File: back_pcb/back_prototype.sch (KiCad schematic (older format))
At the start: 75 parts, among them P1 EXPANSION_LEFT, P2 EXPANSION_BOTTOM, P3 EXPANSION_TOP, P4 USB_A, P5 AUDIO_CONN, P6 ATMEGA_HEADER, P7 EXPANSION_BOTTOM2, P8 JST, P9 USB_A, Q1 IRLML6401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

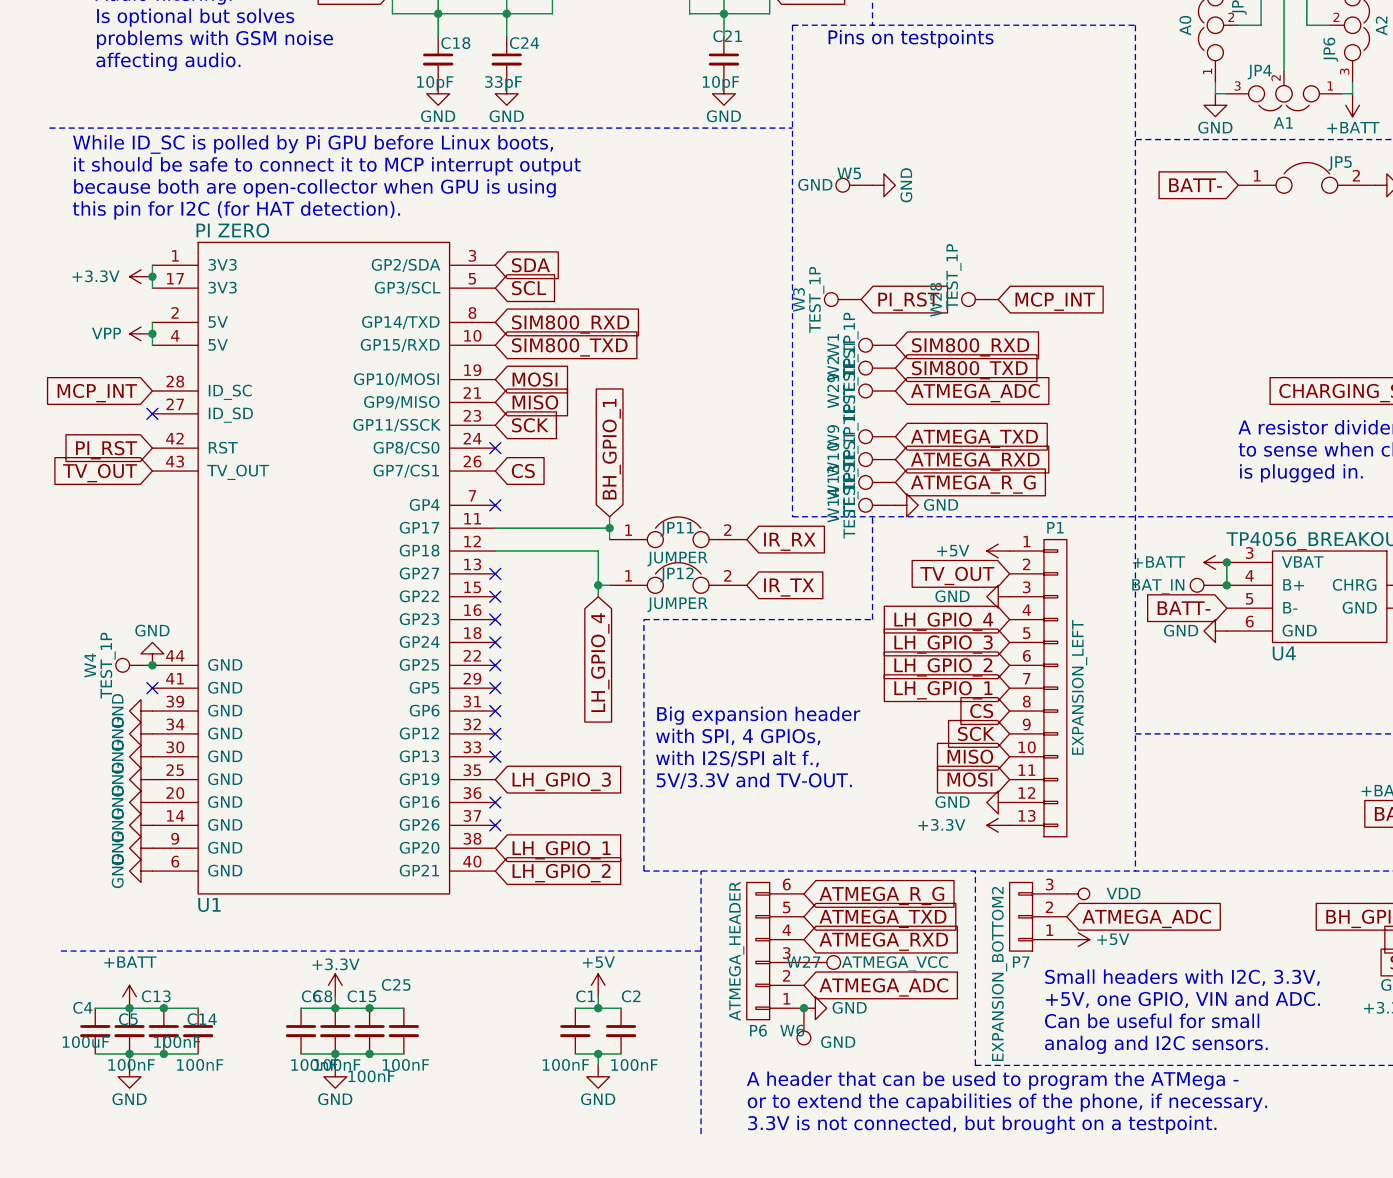
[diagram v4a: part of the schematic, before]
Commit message: Last minute changes in back board
* Added a VSYS capacitor
* Added a capacitor in parallel with the battery
* Removed the MCP_INT testpoint and testpoints for free MCP GPIOs
* Remove the footprint for additional protection IC
* Stitched the board with vias
* Moved the traces around for better grounds
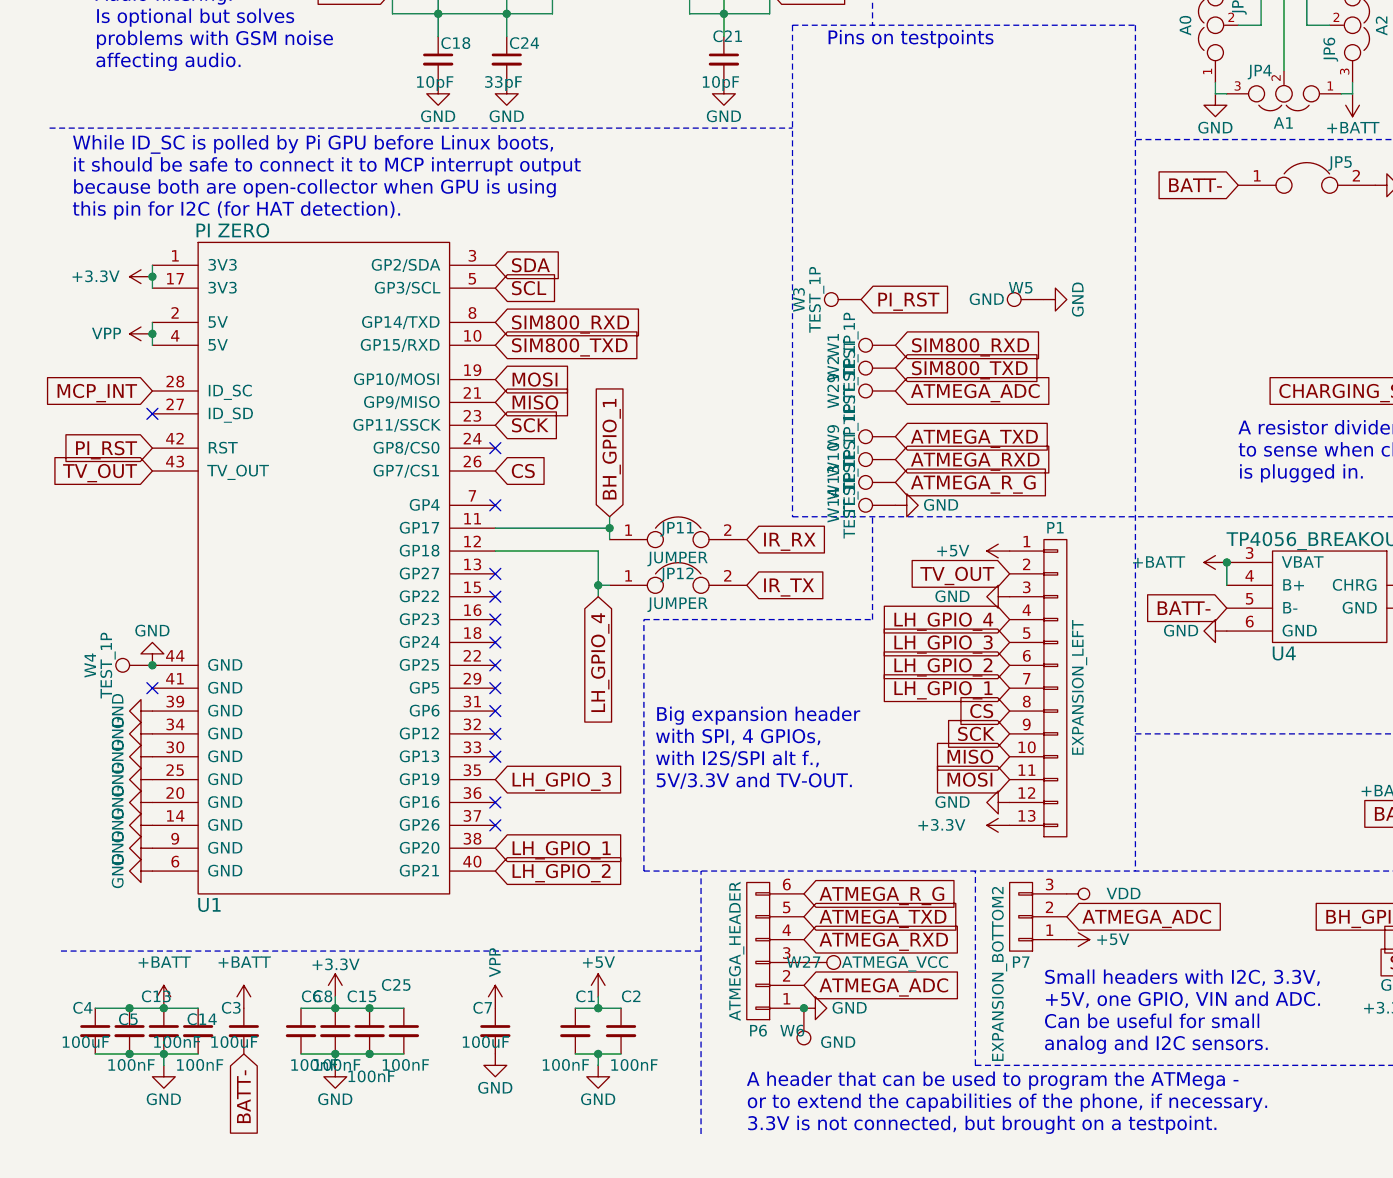
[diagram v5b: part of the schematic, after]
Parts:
- removed W11: BAT_IN, Measurement_Points:Measurement_Point_Square-SMD-Pad_Small, symbol TEST_1P
- removed W28: TEST_1P, Measurement_Points:Measurement_Point_Square-SMD-Pad_Small, symbol TEST_1P
- added C3, C7: 100uF, Capacitors_Tantalum_SMD:CP_Tantalum_Case-B_EIA-3528-21_Hand, symbol C_Small
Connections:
- net +BATT: now also C3.1
- net BATT-: now also C3.2
- net GND: now also C7.2
- net VPP: now also C7.1
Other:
- moved on the sheet: W5
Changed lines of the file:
@@
-	0    -1   -1   0
-$EndComp
-$Comp
-L TEST_1P W11
-U 1 1 5845A9D8
-P 5650 5400
-F 0 "W11" V 5650 5400 50  0001 C CNN
-F 1 "BAT_IN" V 5650 5700 50  0000 C CNN
-F 2 "Measurement_Points:Measurement_Point_Square-SMD-Pad_Small" H 5850 5400 50  0001 C CNN
-F 3 "" H 5850 5400 50  0000 C CNN
-	1    5650 5400
 	0    -1   -1   0
 $EndComp
@@
 L TEST_1P W5
 U 1 1 588B5AFB
-P 4100 3650
-F 0 "W5" V 4150 3750 50  0000 C CNN
-F 1 "GND" V 4100 3900 50  0000 C CNN
-F 2 "Measurement_Points:Measurement_Point_Square-SMD-Pad_Small" H 4300 3650 50  0001 C CNN
-F 3 "" H 4300 3650 50  0000 C CNN
-	1    4100 3650
+P 4850 4150
+F 0 "W5" V 4900 4250 50  0000 C CNN
+F 1 "GND" V 4850 4400 50  0000 C CNN
+F 2 "Measurement_Points:Measurement_Point_Square-SMD-Pad_Small" H 5050 4150 50  0001 C CNN
+F 3 "" H 5050 4150 50  0000 C CNN
+	1    4850 4150
 	0    -1   -1   0
 $EndComp
@@
 $EndComp
 $Comp
-L TEST_1P W28
-U 1 1 588FD363
-P 4650 4150
-F 0 "W28" H 4650 4420 50  0000 C CNN
-F 1 "TEST_1P" H 4750 4350 50  0000 C CNN
-F 2 "Measurement_Points:Measurement_Point_Square-SMD-Pad_Small" H 4850 4150 50  0001 C CNN
-F 3 "" H 4850 4150 50  0000 C CNN
-	1    4650 4150
-	0    -1   -1   0
-$EndComp
-$Comp
 L TEST_1P W29
 U 1 1 588F8B4F
@@
 L GND #PWR050
 U 1 1 58901942
-P 4100 3650
-F 0 "#PWR050" H 4100 3400 50  0001 C CNN
-F 1 "GND" H 4100 3500 50  0000 C CNN
-F 2 "" H 4100 3650 50  0000 C CNN
-F 3 "" H 4100 3650 50  0000 C CNN
-	1    4100 3650
+P 4850 4150
+F 0 "#PWR050" H 4850 3900 50  0001 C CNN
+F 1 "GND" H 4850 4000 50  0000 C CNN
+F 2 "" H 4850 4150 50  0000 C CNN
+F 3 "" H 4850 4150 50  0000 C CNN
+	1    4850 4150
 	0    -1   -1   0
 $EndComp
@@
 Text GLabel 4050 4150 2    60   Input ~ 0
 PI_RST
-Text GLabel 4650 4150 2    60   Input ~ 0
-MCP_INT
 $Comp
 L CONN_01X02 P8
@@
 L +BATT #PWR056
 U 1 1 58911AF4
-P 850 7250
-F 0 "#PWR056" H 850 7100 50  0001 C CNN
-F 1 "+BATT" H 850 7450 50  0000 C CNN
-F 2 "" H 850 7250 50  0000 C CNN
-F 3 "" H 850 7250 50  0000 C CNN
-	1    850  7250
+P 1000 7250
+F 0 "#PWR056" H 1000 7100 50  0001 C CNN
+F 1 "+BATT" H 1000 7450 50  0000 C CNN
+F 2 "" H 1000 7250 50  0000 C CNN
+F 3 "" H 1000 7250 50  0000 C CNN
+	1    1000 7250
 	1    0    0    -1
 $EndComp
@@
 L GND #PWR058
 U 1 1 589168FA
-P 850 7500
-F 0 "#PWR058" H 850 7250 50  0001 C CNN
-F 1 "GND" H 850 7350 50  0000 C CNN
-F 2 "" H 850 7500 50  0000 C CNN
-F 3 "" H 850 7500 50  0000 C CNN
-	1    850  7500
+P 1000 7500
+F 0 "#PWR058" H 1000 7250 50  0001 C CNN
+F 1 "GND" H 1000 7350 50  0000 C CNN
+F 2 "" H 1000 7500 50  0000 C CNN
+F 3 "" H 1000 7500 50  0000 C CNN
+	1    1000 7500
 	1    0    0    -1
 $EndComp
@@
 Wire Wire Line
 	5650 5400 5650 5300
-Connection ~ 5650 5400
 Connection ~ 5650 5300
 Wire Wire Line
@@
 Wire Wire Line
 	8100 6400 8300 6400
-Wire Wire Line
-	700  7250 1150 7250
-Wire Wire Line
-	700  7450 1150 7450
 Wire Wire Line
 	7250 700  7400 700
@@
 Connection ~ 850  7250
 Connection ~ 850  7450
-Wire Wire Line
-	850  7500 850  7450
 Connection ~ 1900 7450
 Connection ~ 1900 7250
@@
 Connection ~ 10100 1650
 Connection ~ 9900 1650
+$Comp
+L C_Small C3
+U 1 1 58D40043
+P 1350 7350
+F 0 "C3" H 1250 7450 50  0000 L CNN
+F 1 "100uF" H 1200 7300 50  0000 L CNN
+F 2 "Capacitors_Tantalum_SMD:CP_Tantalum_Case-B_EIA-3528-21_Hand" H 1350 7350 50  0001 C CNN
+F 3 "" H 1350 7350 50  0000 C CNN
+	1    1350 7350
+	1    0    0    -1
+$EndComp
+$Comp
+L C_Small C7
+U 1 1 58D40155
+P 2450 7350
+F 0 "C7" H 2350 7450 50  0000 L CNN
+F 1 "100uF" H 2300 7300 50  0000 L CNN
+F 2 "Capacitors_Tantalum_SMD:CP_Tantalum_Case-B_EIA-3528-21_Hand" H 2450 7350 50  0001 C CNN
+F 3 "" H 2450 7350 50  0000 C CNN
+	1    2450 7350
+	1    0    0    -1
+$EndComp
+$Comp
+L GND #PWR071
+U 1 1 58D40C19
+P 2450 7450
+F 0 "#PWR071" H 2450 7200 50  0001 C CNN
+F 1 "GND" H 2450 7300 50  0000 C CNN
+F 2 "" H 2450 7450 50  0000 C CNN
+F 3 "" H 2450 7450 50  0000 C CNN
+	1    2450 7450
+	1    0    0    -1
+$EndComp
+$Comp
+L VPP #PWR072
+U 1 1 58D40F5D
+P 2450 7250
+F 0 "#PWR072" H 2450 7100 50  0001 C CNN
+F 1 "VPP" V 2450 7450 50  0000 C CNN
+F 2 "" H 2450 7250 50  0000 C CNN
+F 3 "" H 2450 7250 50  0000 C CNN
+	1    2450 7250
+	1    0    0    -1
+$EndComp
+Wire Wire Line
+	1000 7500 1000 7450
+Wire Wire Line
+	700  7250 1150 7250
+Wire Wire Line
+	1150 7450 700  7450
+$Comp
+L +BATT #PWR073
+U 1 1 58D46D04
+P 1350 7250
+F 0 "#PWR073" H 1350 7100 50  0001 C CNN
+F 1 "+BATT" H 1350 7450 50  0000 C CNN
+F 2 "" H 1350 7250 50  0000 C CNN
+F 3 "" H 1350 7250 50  0000 C CNN
+	1    1350 7250
+	1    0    0    -1
+$EndComp
+Text GLabel 1350 7450 3    60   Input ~ 0
+BATT-
 $EndSCHEMATC

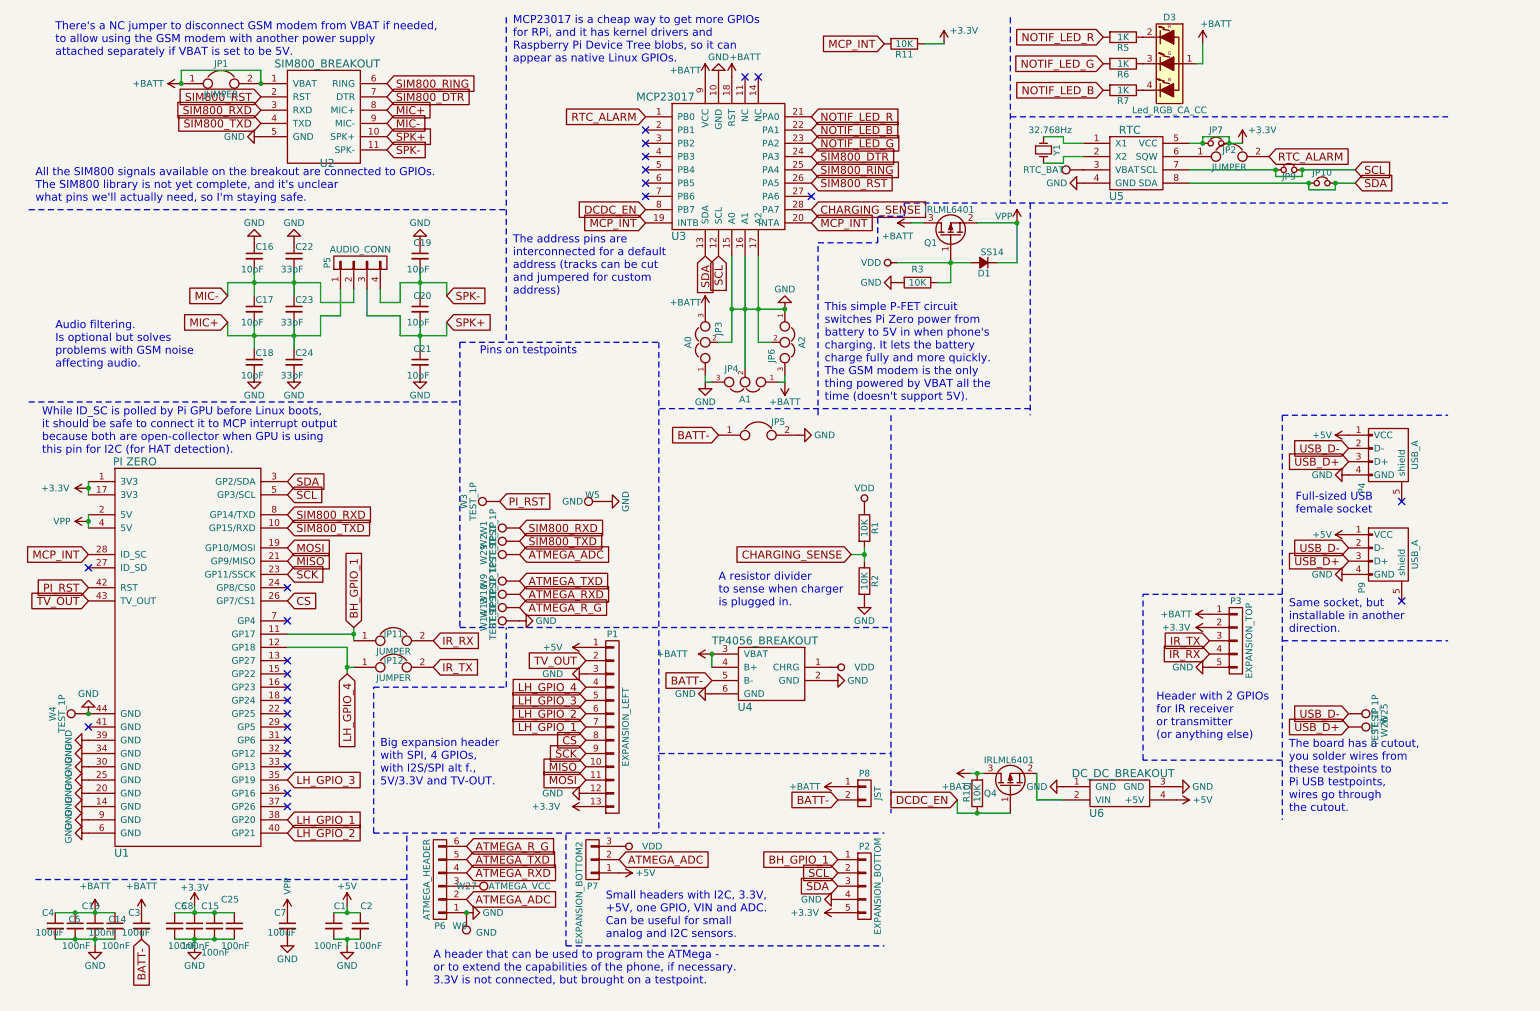
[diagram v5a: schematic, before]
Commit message: Updated back board
* Added a footprint for MPU9050/9150 breakouts
* Added a FET that interrupts VBAT+ and is controlled from GPIO expander
(with a button to reset it?)
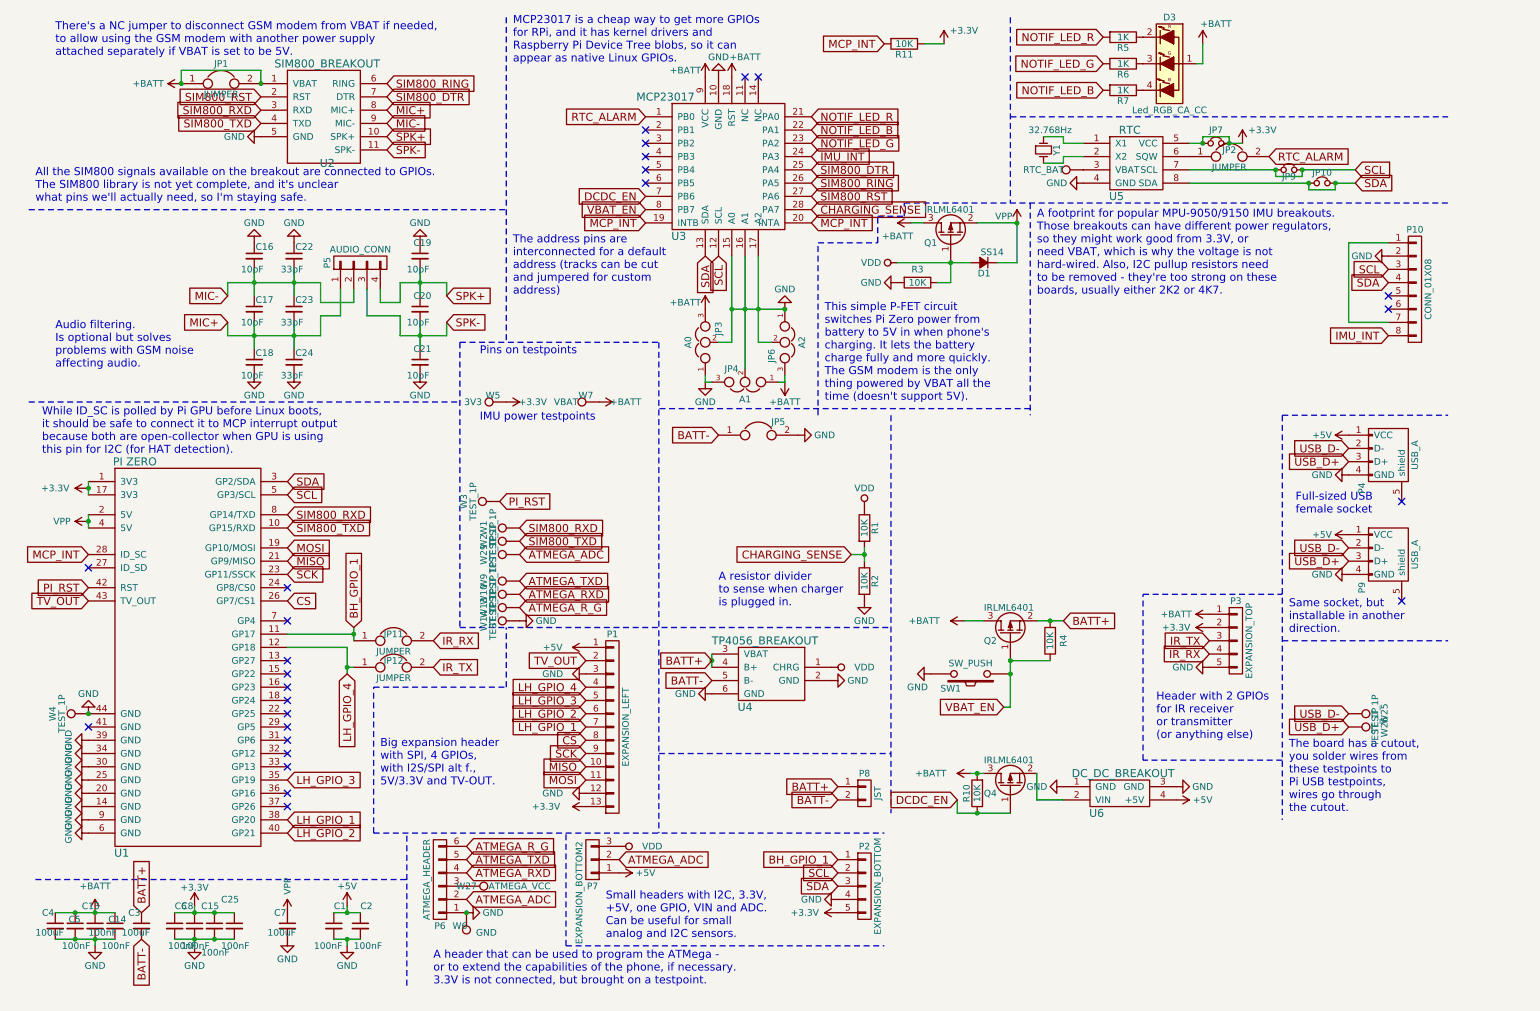
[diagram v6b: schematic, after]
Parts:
- added P10: CONN_01X08, Pin_Headers:Pin_Header_Straight_1x08_Pitch2.54mm, symbol CONN_01X08
- added Q2: IRLML6401, TO_SOT_Packages_SMD:SOT-23_Handsoldering, symbol Q_PMOS_GSD
- added R4: 10K, Resistors_SMD:R_0805_HandSoldering, symbol R
- added SW1: SW_PUSH, footprints:SW_SPST_EVQPE1, symbol SW_PUSH
- added W7: VBAT, Measurement_Points:Measurement_Point_Square-SMD-Pad_Small, symbol TEST_1P
- W5: value GND -> 3V3
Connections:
- net +3V3: now also W5.1
- net +BATT: now also Q2.3 (D), W7.1; no longer C3.1, P8.1 (P1), U4.3 (VBAT), U4.4 (B+)
- net DCDC_EN: now also U3.7 (PB6); no longer U3.8 (PB7)
- net GND: now also P10.2 (P2), SW1.2; no longer W5.1
- net SCL: now also P10.3 (P3)
- net SDA: now also P10.4 (P4)
- net SIM800_DTR: now also U3.25 (PA4); no longer U3.24 (PA3)
- net SIM800_RING: now also U3.26 (PA5); no longer U3.25 (PA4)
- net SIM800_RST: now also U3.27 (PA6); no longer U3.26 (PA5)
- net SPK+: now also C19.2, C20.1, P5.4 (P4); no longer C20.2, C21.1, P5.3 (P3)
- net SPK-: now also C20.2, C21.1, P5.3 (P3); no longer C19.2, C20.1, P5.4 (P4)
- new net: P10.1 (P1), P10.7 (P7)
- new net BATT+: C3.1, P8.1 (P1), Q2.2 (S), R4.2, U4.3 (VBAT), U4.4 (B+)
- new net IMU_INT: P10.8 (P8), U3.24 (PA3)
- new net VBAT_EN: Q2.1 (G), R4.1, SW1.1, U3.8 (PB7)
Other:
- note added: "A footprint for popular MPU-9050/9150 IMU breakouts.\nThose breakouts can have different power regulators,\nso they might work good from 3.3V, or \nneed VBAT, which is why the voltage is not \nhard-wired. Also, I2C pullup resistors need \nto be removed - they're too strong on these \nboards, usually either 2K2 or 4K7."
- note added: "IMU power testpoints"
